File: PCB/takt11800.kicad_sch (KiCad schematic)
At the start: 281 parts, among them J1 Conn_01x05, J3 USB_C, J4 Conn_01x05_Pin, SW1 BOOT, SW2 NRST, U1 STM32F072CBT6, U2 CD74HC4067SM, U3 XC6206, U4 USBLC6-2SC6

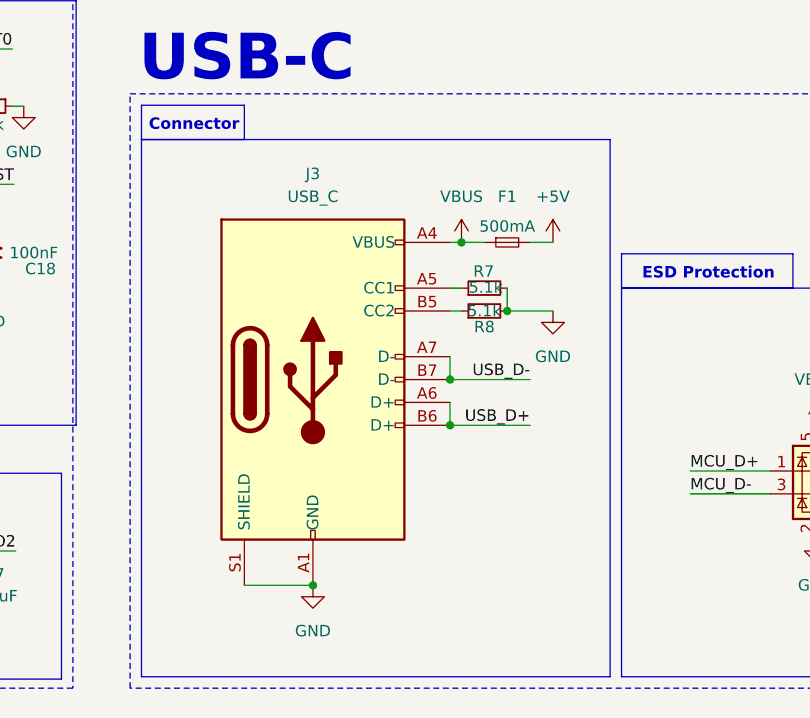
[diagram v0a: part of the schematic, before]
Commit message: update USB-C footprint; adjust arrow keys position; cleanup libraries
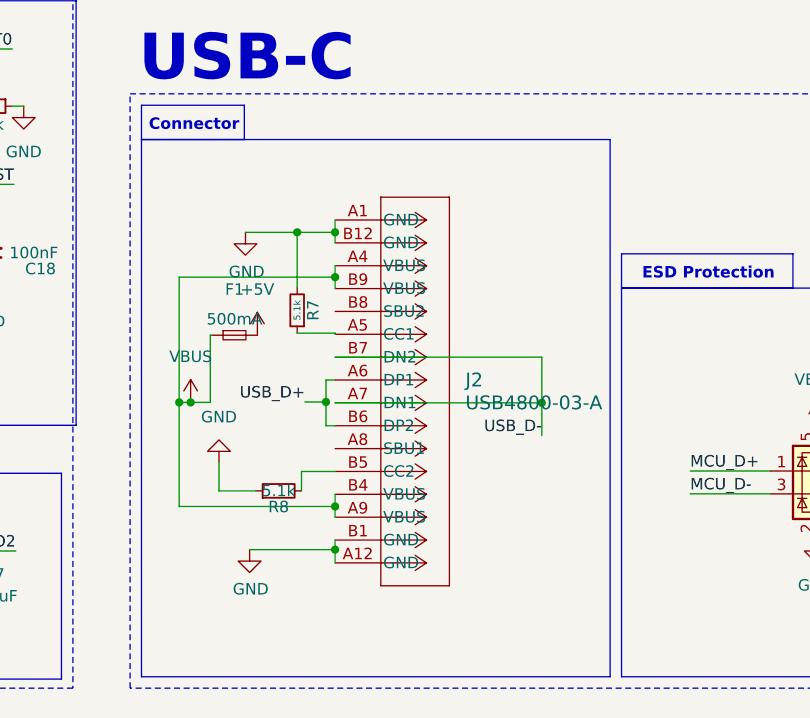
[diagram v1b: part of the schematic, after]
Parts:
- removed J3: USB_C, ScottoKeebs_Components:USB_C_HRO_TYPE-C-31-M-12, symbol Library:USB_C_Receptacle_USB2.0_14P
- added J2: USB4800-03-A, CONN_USB4800_GCT, symbol 2025-06-28_23-31-20:USB4800-03-A
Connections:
- net GND: now also R8.1, J2.A1 (GND), J2.A12 (GND), J2.B1 (GND), J2.B12 (GND); no longer R8.2
- net USB_D+: now also J2.A6 (DP1), J2.B6 (DP2)
- net USB_D-: now also J2.A7 (DN1), J2.B7 (DN2)
- net VBUS: now also J2.A4 (VBUS), J2.A9 (VBUS), J2.B4 (VBUS), J2.B9 (VBUS)
- net at R7.1: now also J2.A5 (CC1)
- new net: J2.B5 (CC2), R8.2
